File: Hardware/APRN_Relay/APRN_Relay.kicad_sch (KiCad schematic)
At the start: 29 parts, among them J101 Pi_Zero, J102 SERVO1, J103 SERVO2, J104 PTT, J105 RADIO, J106 CHG_IN, U101 DHT11, U102 NCV1117ST50T3G

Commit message: Plz fix?
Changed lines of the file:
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@@
   (junction (at 142.875 133.985) (diameter 0) (color 0 0 0 0)
+  )
+  (junction (at 277.495 52.07) (diameter 0) (color 0 0 0 0)
   )
   (junction (at 228.6 24.13) (diameter 0) (color 0 0 0 0)
@@
     )
     (property "Datasheet" "" (id 3) (at 247.65 52.705 0)
+      (effects (font (size 1.27 1.27)) hide)
+    )
+    (pin "1")
+  )
+  (symbol (lib_id "power:PWR_FLAG") (at 277.495 52.07 270) (unit 1)
+    (in_bom yes) (on_board yes) (fields_autoplaced)
+    (property "Reference" "#FLG?" (id 0) (at 279.4 52.07 0)
+      (effects (font (size 1.27 1.27)) hide)
+    )
+    (property "Value" "PWR_FLAG" (id 1) (at 282.575 52.07 0)
+      (effects (font (size 1.27 1.27)) hide)
+    )
+    (property "Footprint" "" (id 2) (at 277.495 52.07 0)
+      (effects (font (size 1.27 1.27)) hide)
+    )
+    (property "Datasheet" "~" (id 3) (at 277.495 52.07 0)
       (effects (font (size 1.27 1.27)) hide)
     )
@@
       (reference "#FLG0102") (unit 1) (value "PWR_FLAG") (footprint "")
     )
+    (path "/18ab2efb-7eb4-498a-b682-ad87b4f1abe9"
+      (reference "#FLG?") (unit 1) (value "PWR_FLAG") (footprint "")
+    )
     (path "/e3a2244a-1b20-4762-a809-e6b3c0953a39"

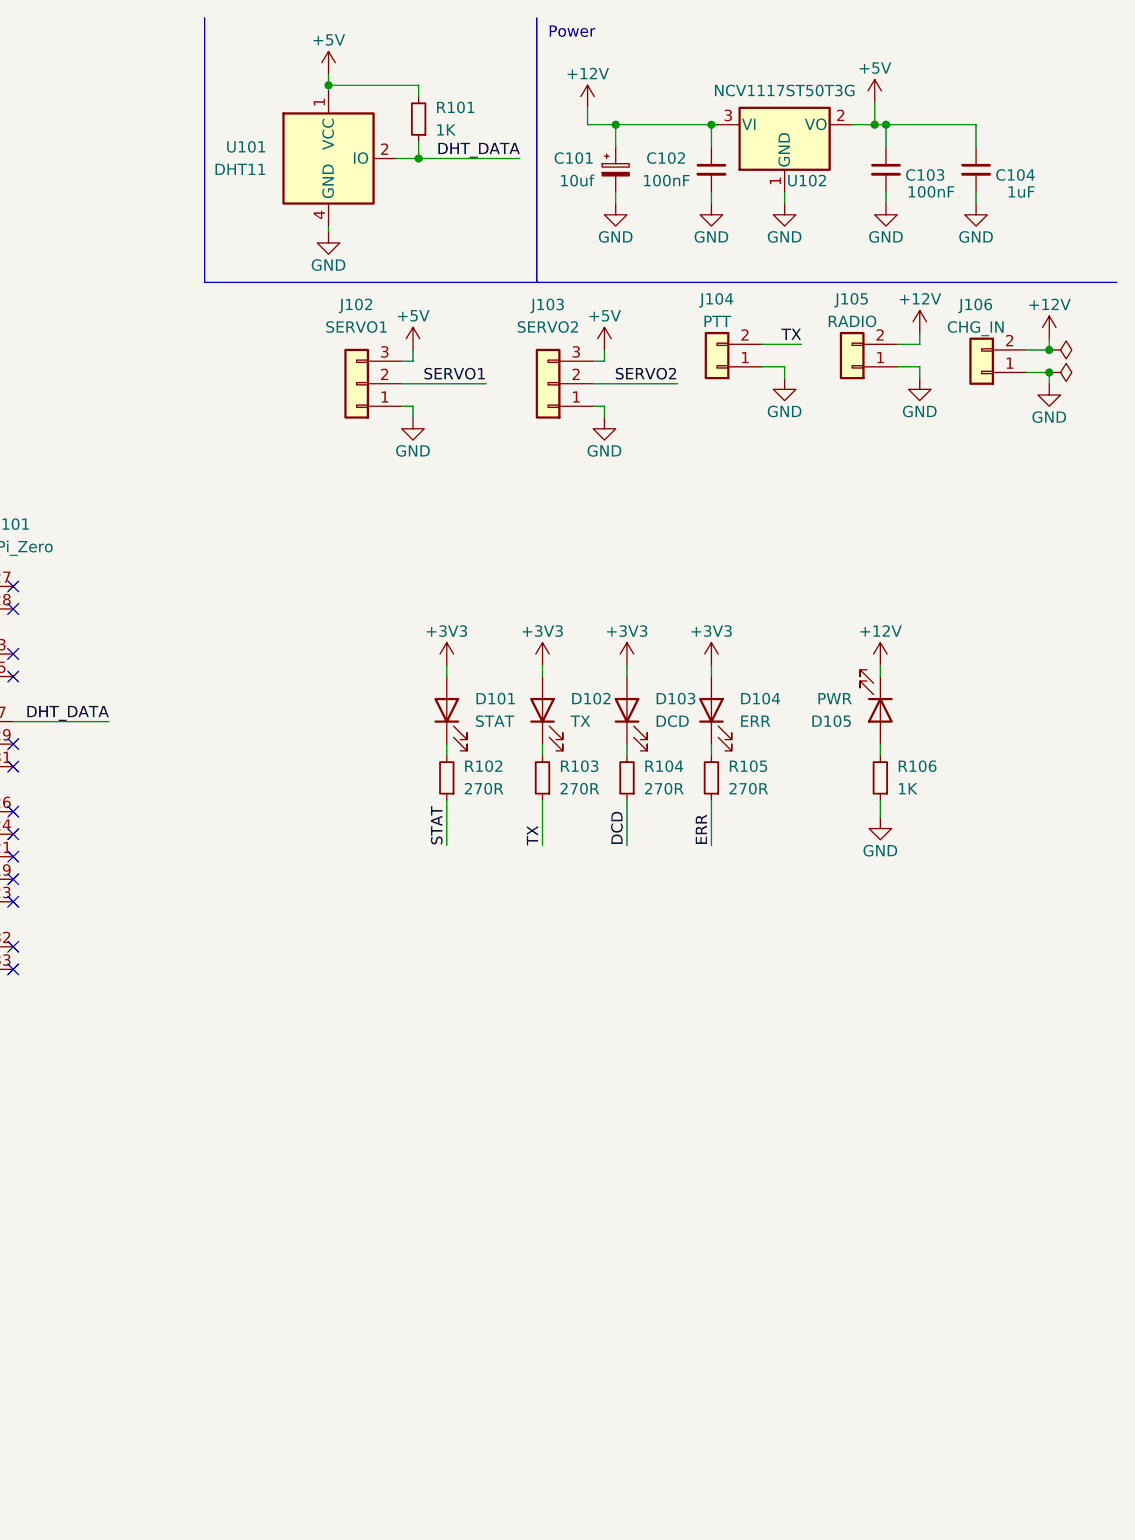
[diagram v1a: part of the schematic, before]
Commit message: Add pi 3d model
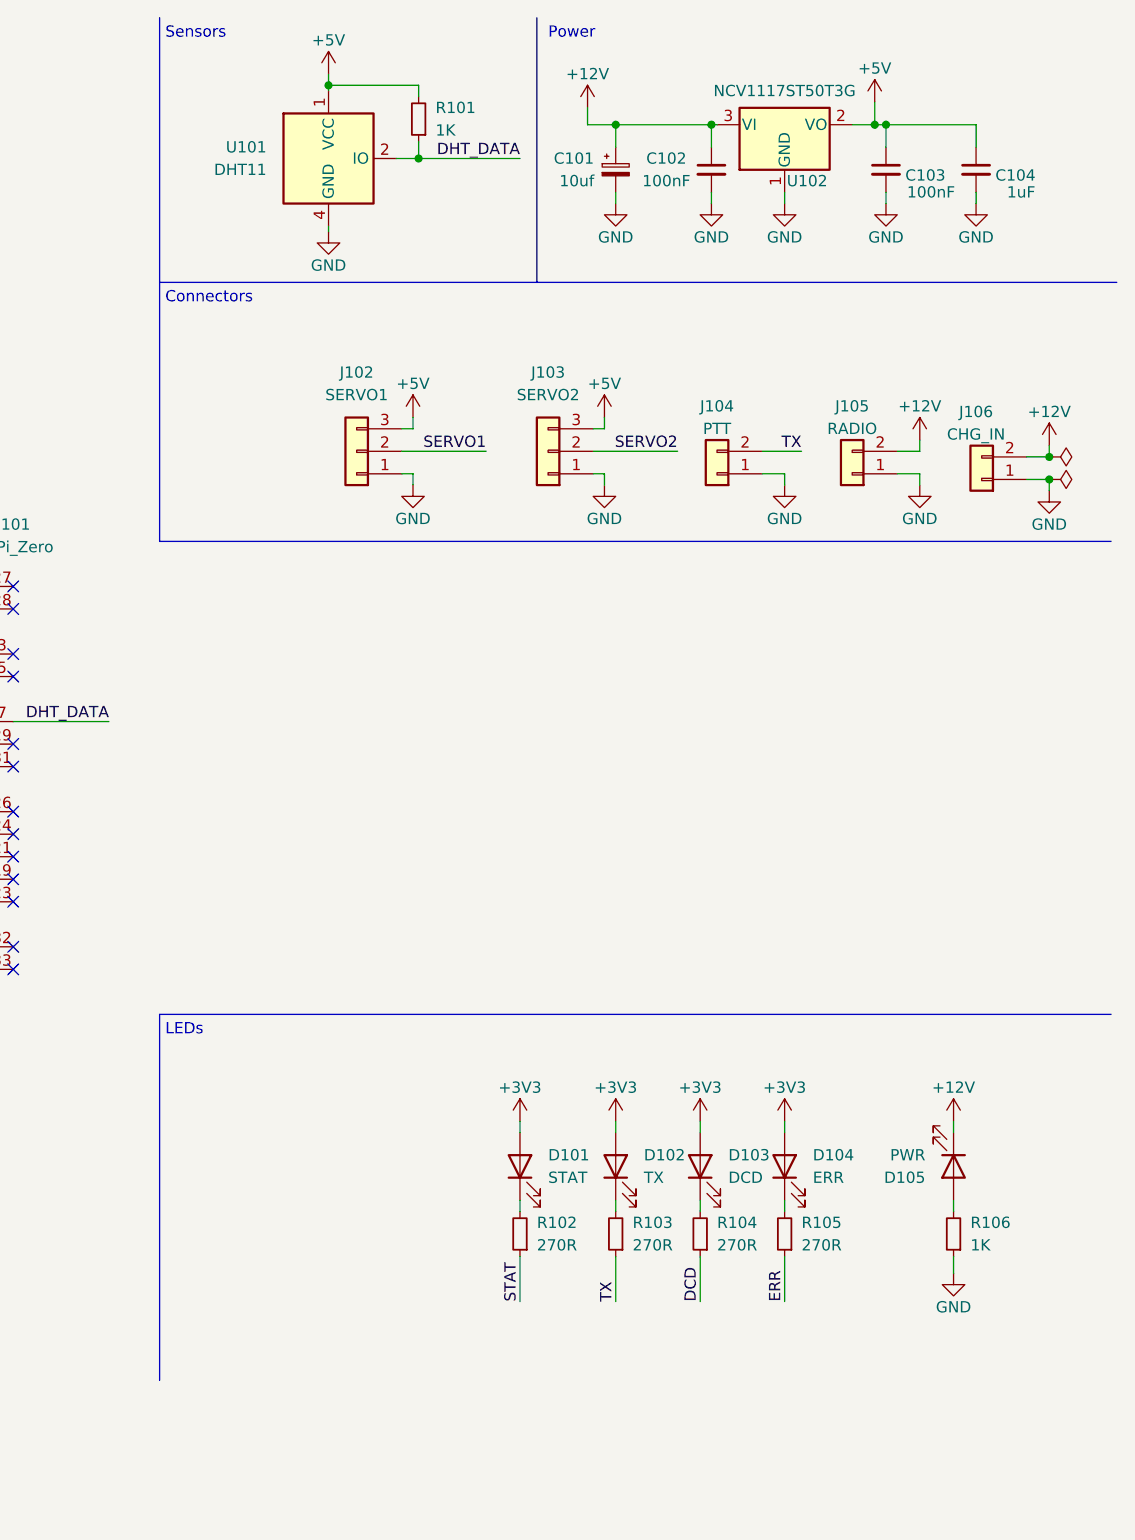
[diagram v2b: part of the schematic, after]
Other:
- note added: "Connectors"
- note added: "LEDs"
- note added: "Sensors"
- moved on the sheet: D101, D102, D103, D104, D105, J102, J103, J104, J105, J106, R102, R103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

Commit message: Clean the last bits and prep for a tidy final review series, merge into 1.0 when done
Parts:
- added C101: 1uF, Capacitor_SMD:C_0805_2012Metric, symbol Device:C_Small
- added JP101: A1, Jumper:SolderJumper-2_P1.3mm_Open_TrianglePad1.0x1.5mm, symbol Jumper:SolderJumper_2_Open
- added JP102: A0, Jumper:SolderJumper-2_P1.3mm_Open_TrianglePad1.0x1.5mm, symbol Jumper:SolderJumper_2_Open
- added R103: 100R, Resistor_SMD:R_2512_6332Metric, symbol Device:R_Small
- added R107, R108, R110, R111: 10k, Resistor_SMD:R_0805_2012Metric, symbol Device:R_Small
- added U102: INA219AIDR, Package_SO:SOIC-8_3.9x4.9mm_P1.27mm, symbol Analog_ADC:INA219AxD
- renumbered C101 to C102, C102 to C103, C103 to C104, C104 to C105, R103 to R104, R104 to R105, R105 to R106, R106 to R109, U102 to U103
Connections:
- net +12V: now also R103.2, U102.8 (IN+); no longer C102.1, C103.1, J105.2 (Pin_2), U103.3 (VI)
- net +5V: now also C101.1, JP101.1 (A), JP102.1 (A), R107.2, R110.2, U102.5 (VS)
- net GND: now also C101.2, R108.1, R111.1, U102.6 (GND)
- net STAT: now also J101.15 (GPIO22); no longer J101.37 (GPIO26)
- net SDA: now reaches J101.3 (SDA/GPIO2)
- net SDA: now also R107.1, U102.3 (SDA)
- net SCL: now reaches J101.5 (SCL/GPIO3)
- net SCL: now also R110.1, U102.4 (SCL)
- new net A0: JP102.2 (B), R111.2, U102.2 (A0)
- new net A1: JP101.2 (B), R108.2, U102.1 (A1)
- new net PWR_IN: C102.1, C103.1, J105.2 (Pin_2), R103.1, U102.7 (IN-), U103.3 (VI)
- no-connect marks 22 -> 20
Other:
- note added: "Power Metering"
- moved on the sheet: C102, C103, C104, C105, U103

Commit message: Add power flag to other side of load resistor
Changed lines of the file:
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@@
     (company "Kitsune Scientific")
+  )
+  (junction (at 234.95 102.87) (diameter 0) (color 0 0 0 0)
   )
   (junction (at 135.255 64.77) (diameter 0) (color 0 0 0 0)
@@
     (stroke (width 0) (type default) (color 0 0 0 0))
   )
+  (wire (pts (xy 234.95 102.87) (xy 236.22 102.87))
+    (stroke (width 0) (type default) (color 0 0 0 0))
+  )
   (wire (pts (xy 274.955 80.645) (xy 274.955 83.185))
     (stroke (width 0) (type default) (color 0 0 0 0))
@@
     (stroke (width 0) (type default) (color 0 0 0 0))
   )
-  (wire (pts (xy 224.79 102.87) (xy 236.22 102.87))
+  (wire (pts (xy 224.79 102.87) (xy 234.95 102.87))
     (stroke (width 0) (type default) (color 0 0 0 0))
   )
@@
     )
     (property "Datasheet" "" (id 3) (at 217.805 136.525 0)
+      (effects (font (size 1.27 1.27)) hide)
+    )
+    (pin "1")
+  )
+  (symbol (lib_id "power:PWR_FLAG") (at 234.95 102.87 0) (unit 1)
+    (in_bom yes) (on_board yes) (fields_autoplaced)
+    (property "Reference" "#FLG0104" (id 0) (at 234.95 100.965 0)
+      (effects (font (size 1.27 1.27)) hide)
+    )
+    (property "Value" "PWR_FLAG" (id 1) (at 234.95 97.79 0)
+      (effects (font (size 1.27 1.27)) hide)
+    )
+    (property "Footprint" "" (id 2) (at 234.95 102.87 0)
+      (effects (font (size 1.27 1.27)) hide)
+    )
+    (property "Datasheet" "~" (id 3) (at 234.95 102.87 0)
       (effects (font (size 1.27 1.27)) hide)
     )
@@
       (reference "#FLG0103") (unit 1) (value "PWR_FLAG") (footprint "")
     )
+    (path "/61c58c11-2766-4dd4-9607-4af59e4f7fa0"
+      (reference "#FLG0104") (unit 1) (value "PWR_FLAG") (footprint "")
+    )
     (path "/e3a2244a-1b20-4762-a809-e6b3c0953a39"

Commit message: make shunt resistor value more clear
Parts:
- R103: value 100R -> 0.1Ω
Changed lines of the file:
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@@
       (effects (font (size 1.27 1.27)) (justify right))
     )
-    (property "Value" "100R" (id 1) (at 226.695 101.6 0)
+    (property "Value" "0.1Ω" (id 1) (at 226.695 101.6 0)
       (effects (font (size 1.27 1.27)) (justify right))
     )
@@
     )
     (path "/f13ded33-56f4-4c39-b1ce-9d4fbf5b36f5"
-      (reference "R103") (unit 1) (value "100R") (footprint "Resistor_SMD:R_2512_6332Metric")
+      (reference "R103") (unit 1) (value "0.1Ω") (footprint "Resistor_SMD:R_2512_6332Metric")
     )
     (path "/d06e768f-7379-46b4-bd72-628e1fe49db1"

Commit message: INA219 and I2C lines now driven by 3.3v instead of 5.0v
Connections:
- net +3V3: now also C101.1, J101.1 (3V3), R107.2, R110.2, U102.5 (VS)
- net +5V: no longer C101.1, R107.2, R110.2, U102.5 (VS)
- net GND: no longer J101.14 (GND), J101.6 (GND)
- no-connect marks 20 -> 21

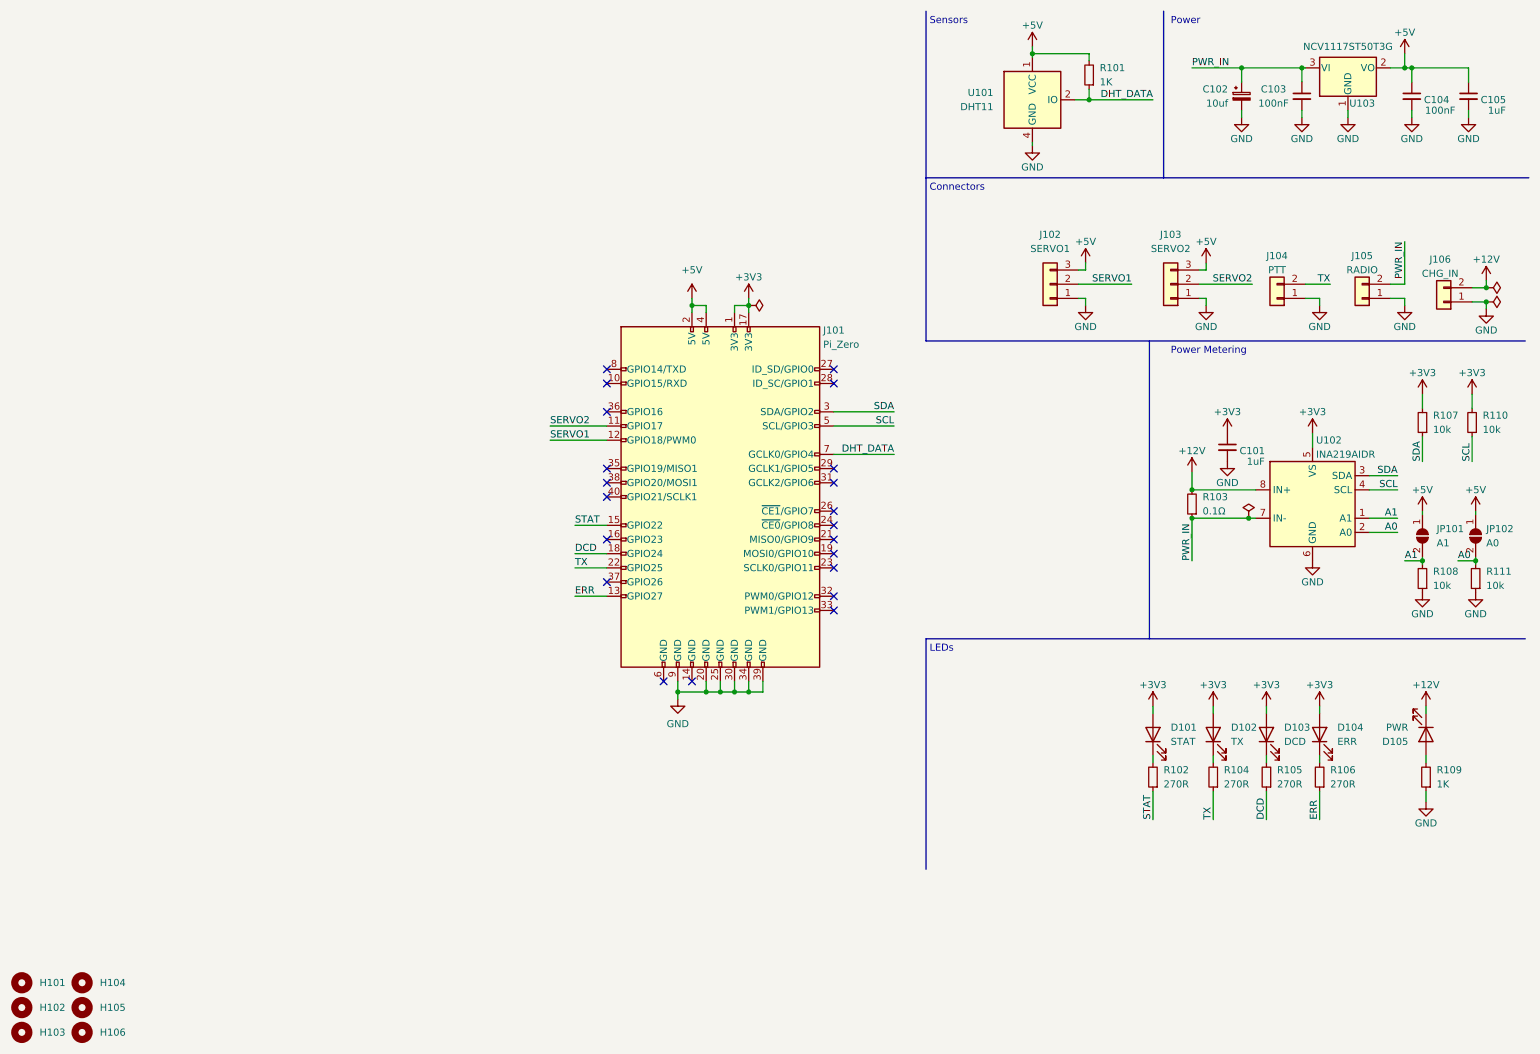
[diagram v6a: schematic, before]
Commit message: Implement changes from dad
Co-Authored By: ka2qfx
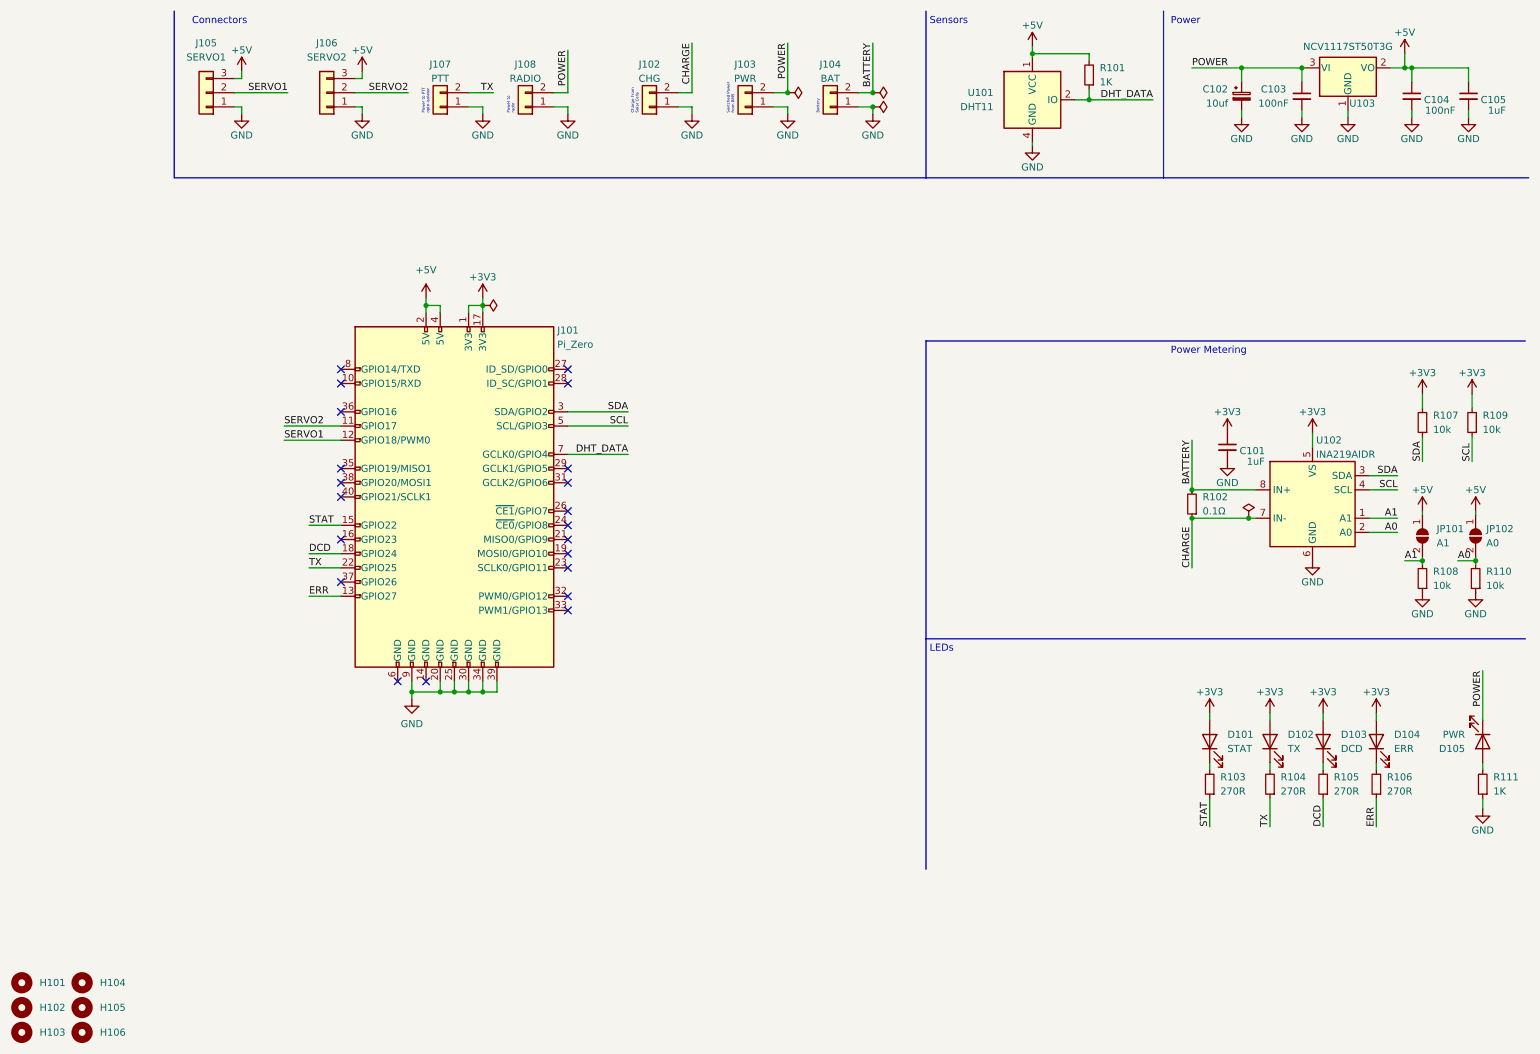
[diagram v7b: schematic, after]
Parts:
- added J103: PWR, Connector_JST:JST_EH_S2B-EH_1x02_P2.50mm_Horizontal, symbol Connector_Generic:Conn_01x02
- added J104: BAT, Connector_JST:JST_EH_S2B-EH_1x02_P2.50mm_Horizontal, symbol Connector_Generic:Conn_01x02
- J102: renamed from J106; value CHG_IN -> CHG
- renumbered J102 to J105, J103 to J106, J104 to J107, J105 to J108, R103 to R102, R102 to R103, R110 to R109, R111 to R110, R109 to R111
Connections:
- net GND: now also J103.1 (Pin_1), J104.1 (Pin_1)
- net +12V renamed BATTERY
- net BATTERY: now also J104.2 (Pin_2); no longer D105.1 (K), J102.2 (Pin_2)
- net PWR_IN renamed POWER
- net POWER: now also D105.1 (K), J103.2 (Pin_2); no longer R102.1, U102.7 (IN-)
- new net CHARGE: J102.2 (Pin_2), R102.1, U102.7 (IN-)
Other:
- note added: "Battery"
- note added: "Charge From Solar Cells"
- note added: "Power to PTT opto-isolator"
- note added: "Power to radio"
- note added: "Switched Power from BMS"
- moved on the sheet: D101, D102, D103, D104, D105, J101, J102, J105, J106, J107, J108, R103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

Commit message: Include last changes from dad, thanks!
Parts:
- added JP101: PWR_BYPAS, Jumper:SolderJumper-2_P1.3mm_Open_TrianglePad1.0x1.5mm, symbol Jumper:SolderJumper_2_Open
- R103, R104, R105, R106: value 270R -> 330R
- renumbered J105 to J101, J106 to J102, J107 to J103, J101 to J104, J108 to J105, J102 to J106, J103 to J107, J104 to J108, JP101 to JP102, JP102 to JP103
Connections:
- net +3V3: no longer D101.2 (A), D102.2 (A), D103.2 (A), D104.2 (A)
- net BATTERY: now also R102.1, U102.7 (IN-), JP101.2 (B); no longer R102.2, U102.8 (IN+)
- net CHARGE: now also R102.2, U102.8 (IN+); no longer R102.1, U102.7 (IN-)
- net DCD: now also D103.2 (A); no longer R105.1
- net ERR: now also D104.2 (A); no longer R106.1
- net GND: now also R103.1, R104.1, R105.1, R106.1
- net POWER: now also D105.2 (A), JP101.1 (A); no longer D105.1 (K)
- net STAT: now also D101.2 (A); no longer R103.1
- net TX: now also D102.2 (A); no longer R104.1
- net at R111.2: now also D105.1 (K); no longer D105.2 (A)
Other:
- moved on the sheet: D101, D102, D103, D104, D105, R103, R104, R105, R106, R111
